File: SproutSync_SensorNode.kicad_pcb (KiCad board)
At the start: 4 copper layers, 41 x 82.3 mm, 53 parts, among them J1 10132798-031100LF, J2 10132798-031100LF, J3 OSTVN04A150, J4 3-2199250-4, J5 3-2199250-4, J6 OSTVN02A150, J7 Conn_01x03, Q1 PMH950UPEH, Q2 AS2302, Q3 PMH950UPEH, Q5 PMH950UPEH, U1 LTR-329ALS-01, U2 SHT40-AD1F-R2, U3 ZMOD4410AI1R, U4 SN75176BDR, U5 AP63205WU-7, U7 MCP1700T-3302E/TT, U8 74HC04D

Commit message: 2nd rev schematic done
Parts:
- moved C9 36.1 mm to (101.9, 114.7)
- moved U7 35.2 mm to (101.8, 112.3)
- moved C10 35.2 mm to (99.2, 112.2)
- moved D4 31.4 mm to (83.3, 105.2)
- moved D5 31.4 mm to (83.3, 104.0)
- moved R2 31.4 mm to (81.2, 105.2)
- moved R6 31.4 mm to (81.2, 104.0)
- moved U3 10.6 mm to (106.6, 109.7)
- moved Q3 9.95 mm to (103.8, 110.6), turned to 0 degrees
- moved C2 7.49 mm to (107.5, 112.0), turned to 180 degrees
- moved U1 5.01 mm to (112.2, 109.4), turned to 90 degrees
- moved C8 4.63 mm to (119.1, 93.2)
- moved U2 4.39 mm to (109.6, 109.6), turned to -90 degrees
- moved C1 4.09 mm to (112.7, 111.5), turned to 0 degrees
- moved R3 1.61 mm to (111.3, 104.1)
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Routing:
- net /PetalStackingConectors/PAD32: track 1.15 -> 35.8 mm
- net /PetalStackingConectors/PAD33: track 1.64 -> 31.0 mm
- net +5V: track 15.2 -> 36.9 mm
- net Sns_3p3: track 0.00 -> 18.7 mm
- net /PetalStackingConectors/PAD30: track 0.00 -> 18.4 mm
- net WRT_ENA: track 0.00 -> 14.6 mm
- net /PetalStackingConectors/PAD31: track 0.00 -> 13.6 mm
- net D: track 0.00 -> 11.6 mm
- net RS485_B-: track 0.00 -> 10.6 mm
- net R: track 0.00 -> 10.2 mm
- net RS485_A+: track 0.00 -> 9.54 mm
- net RX: track 0.00 -> 8.55 mm
- net TX: track 0.00 -> 6.00 mm
- net +3V3: track 0.00 -> 5.85 mm
- net RE/DE: track 0.00 -> 5.17 mm
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
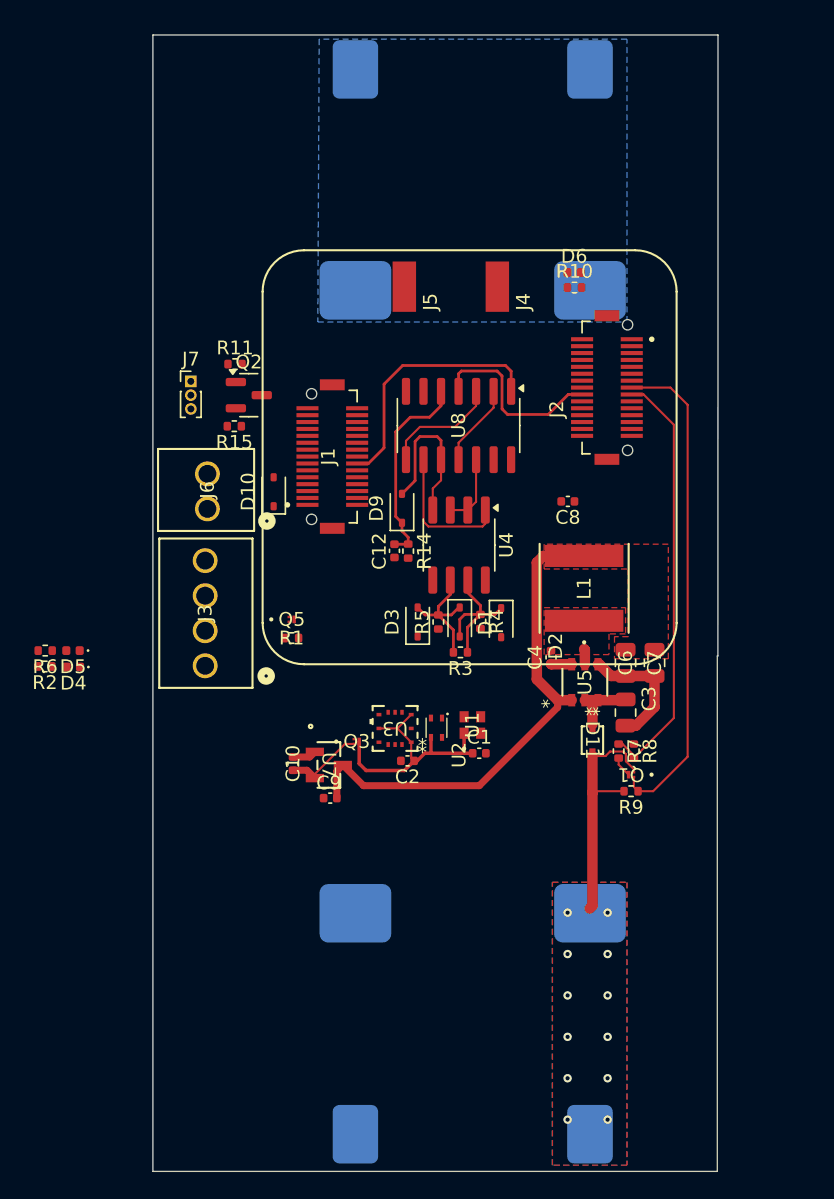
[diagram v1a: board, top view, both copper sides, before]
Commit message: mostly routed
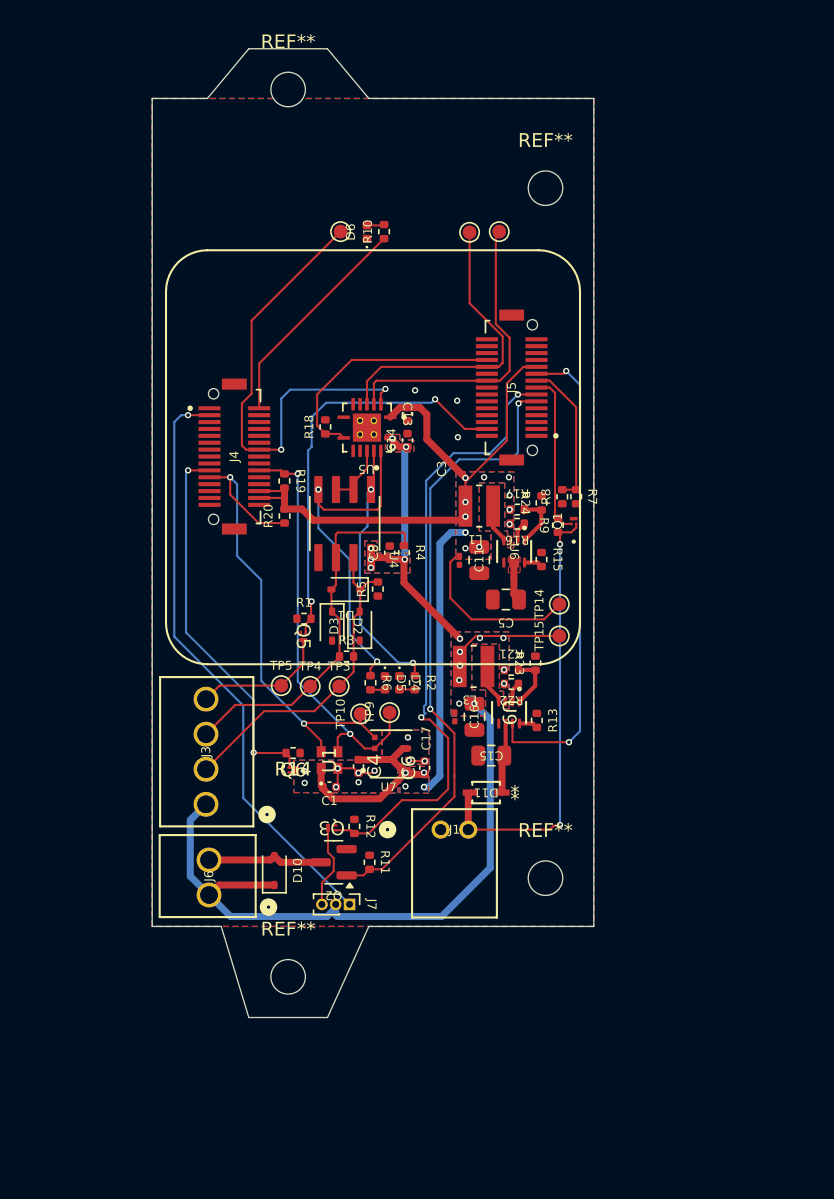
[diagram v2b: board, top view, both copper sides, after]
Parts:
- removed BT2, BT3: Battery_Cell, SproutSenseFootprints:Keystone_18650_Holder
- removed C10, C2, C9: 1uF, Capacitor_SMD:C_0402_1005Metric
- removed C12: 100nF, Capacitor_SMD:C_0402_1005Metric
- removed C7: 22uF, Capacitor_SMD:C_0805_2012Metric
- removed D9: 1N4148WS, Diode_SMD:D_SOD-323
- removed J2: 10132798-031100LF, SproutSenseFootprints:AMPHENOL_10132798-031100LF
- removed U2: SHT40-AD1F-R2, SproutSenseFootprints:SHT4X
- removed U3: ZMOD4410AI1R, SproutSenseFootprints:QFN_410AI1R_REN
- removed U8: 74HC04D, Package_SO:SOIC-14_3.9x8.7mm_P1.27mm
- added C11: 22uF, Capacitor_SMD:C_0805_2012Metric, F.Cu at (112.7, 97.5)
- added C13: 1uF, Capacitor_SMD:C_0402_1005Metric, F.Cu at (107.5, 86.9)
- added C14: 1uF, Capacitor_SMD:C_0402_1005Metric, F.Cu at (107.5, 88.8)
- added C15: 22uF, Capacitor_SMD:C_0805_2012Metric, F.Cu at (113.6, 111.6)
- added C16: 22uF, Capacitor_SMD:C_0805_2012Metric, F.Cu at (112.4, 108.8)
- added C17: 10n, Capacitor_SMD:C_0201_0603Metric, F.Cu at (110.9, 108.8)
- added C5: 22uF, Capacitor_SMD:C_0805_2012Metric, F.Cu at (114.6, 100.3)
- added L3: 2.2u, SproutSenseFootprints:IND_VLS3012CX-2R2M-1, F.Cu at (112.3, 105.2)
- added Q6: SIUD412ED-T1-GE3, SproutSenseFootprints:SMT_412ED-T1-GE3_VIS, F.Cu at (99.2, 112.7)
- added R12: 4.7k, Resistor_SMD:R_0402_1005Metric, F.Cu at (103.7, 116.8)
- added R13: 9.31k, Resistor_SMD:R_0402_1005Metric, F.Cu at (116.9, 109.1)
- added R16: 100k, Resistor_SMD:R_0402_1005Metric, F.Cu at (115.5, 94.8)
- added R17: 154k, Resistor_SMD:R_0402_1005Metric, F.Cu at (115.5, 93.8)
- added R18: 4.7k, Resistor_SMD:R_0402_1005Metric, F.Cu at (101.5, 87.8)
- added R19: 4.7k, Resistor_SMD:R_0402_1005Metric, F.Cu at (98.6, 91.7)
- added R20: 4.7k, Resistor_SMD:R_0402_1005Metric, F.Cu at (98.6, 94.3)
- added R21: 249k, Resistor_SMD:R_0402_1005Metric, F.Cu at (115.0, 105.4)
- added R22: 100k, Resistor_SMD:R_0402_1005Metric, F.Cu at (115.0, 106.4)
- added R23: 34k, Resistor_SMD:R_0402_1005Metric, F.Cu at (116.8, 104.9)
- added R24: 34k, Resistor_SMD:R_0402_1005Metric, F.Cu at (117.2, 93.3)
- added REF**: MountingHole_2.5mm, MountingHole:MountingHole_2.5mm, F.Cu at (98.8, 127.7)
- added REF**: MountingHole_2.5mm, MountingHole:MountingHole_2.5mm, F.Cu at (98.8, 63.4)
- added REF**: MountingHole_2.5mm, MountingHole:MountingHole_2.5mm, F.Cu at (117.5, 120.5)
- added REF**: MountingHole_2.5mm, MountingHole:MountingHole_2.5mm, F.Cu at (117.5, 70.5)
- added TP1: TestPoint, TestPoint:TestPoint_Pad_D1.0mm, F.Cu at (114.2, 73.7)
- added TP10: TestPoint, TestPoint:TestPoint_Pad_D1.0mm, F.Cu at (104.1, 108.6)
- added TP14: TestPoint, TestPoint:TestPoint_Pad_D1.0mm, F.Cu at (118.5, 100.7)
- added TP15: TestPoint, TestPoint:TestPoint_Pad_D1.0mm, F.Cu at (118.5, 103.0)
- added TP2: TestPoint, TestPoint:TestPoint_Pad_D1.0mm, F.Cu at (102.7, 73.7)
- added TP3: TestPoint, TestPoint:TestPoint_Pad_D1.0mm, F.Cu at (102.5, 106.6)
- added TP4: TestPoint, TestPoint:TestPoint_Pad_D1.0mm, F.Cu at (100.5, 106.6)
- added TP5: TestPoint, TestPoint:TestPoint_Pad_D1.0mm, F.Cu at (98.3, 106.5)
- added TP6: TestPoint, TestPoint:TestPoint_Pad_D1.0mm, F.Cu at (112.0, 73.7)
- added TP9: TestPoint, TestPoint:TestPoint_Pad_D1.0mm, F.Cu at (106.2, 108.5)
- added U6: TPS629203DRL, SproutSenseFootprints:SOT5X3-8_DRL_TEX, F.Cu at (115.2, 96.8)
- added U9: TPS629206DRLR, SproutSenseFootprints:SOT5X3-8_DRL_TEX, F.Cu at (114.9, 108.5)
- C3: value 22uF -> 10n; footprint Capacitor_SMD:C_0805_2012Metric -> Capacitor_SMD:C_0201_0603Metric
- C6: value 22uF -> 100nF; footprint Capacitor_SMD:C_0805_2012Metric -> Capacitor_SMD:C_0402_1005Metric
- C8: value 100nF -> 1uF
- J1: value 10132798-031100LF -> S2B-PH-K-S; footprint SproutSenseFootprints:AMPHENOL_10132798-031100LF -> SproutSenseFootprints:CONN_S2B-PH-K-S_JST
- J4, J5: value 3-2199250-4 -> 10132797-031100LF; footprint SproutSenseFootprints:TE_3-2199250-4 -> SproutSenseFootprints:AMPHENOL_10132797-031100LF
- L1: value 4.7uH -> 2.2u; footprint SproutSenseFootprints:IND_TAIYO_NRS6028_TAY -> SproutSenseFootprints:IND_VLS3012CX-2R2M-1
- Q3, Q5: value PMH950UPEH -> SIUD412ED-T1-GE3; footprint SproutSenseFootprints:QPMOS1G2S3d_SOT8001_NEX -> SproutSenseFootprints:SMT_412ED-T1-GE3_VIS
- R10, R2, R6: value 4.7k -> 1k
- R14: value 22k -> 4.7k
- R15, R7: value 4.7k -> 7.5k
- U4: value SN75176BDR -> SN65HVD3082EDR; footprint Package_SO:SOP-8_3.76x4.96mm_P1.27mm -> SproutSenseFootprints:SOIC127P599X175-8N
- U5: value AP63205WU-7 -> TXB0104RGYR; footprint SproutSenseFootprints:SOIC_05WU-7_DIO -> SproutSenseFootprints:QFN50P350X350X100-15N
- U7: value MCP1700T-3302E/TT -> BME688; footprint SproutSenseFootprints:SOT-23_MC_MCH -> SproutSenseFootprints:IC_BME688
- moved J7 39.6 mm to (103.3, 122.4), turned to -90 degrees
- moved R11 37.4 mm to (104.8, 119.3), turned to 90 degrees
- moved Q2 34.4 mm to (102.2, 119.3), turned to 180 degrees
- moved J1 28.2 mm to (109.9, 117.0), turned to 0 degrees
- moved J6 28.0 mm to (93.1, 121.7)
- moved D10 27.5 mm to (97.8, 120.0)
- moved R2 26.8 mm to (108.0, 106.3), turned to -90 degrees
- moved U5 24.3 mm to (104.6, 87.8), turned to 180 degrees
- moved R15 24.3 mm to (117.2, 97.4), turned to -90 degrees
- moved R6 23.7 mm to (104.8, 106.3), turned to -90 degrees
- moved D4 23.7 mm to (106.9, 106.3), turned to -90 degrees
- moved D5 22.7 mm to (105.9, 106.3), turned to -90 degrees
- moved J4 22.7 mm to (95.0, 90.0), turned to 90 degrees
- moved R9 20.0 mm to (118.4, 94.9), turned to -90 degrees
- moved R8 19.1 mm to (118.7, 92.9), turned to 90 degrees
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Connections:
- C1 pad 1: Sns_3p3 -> +3V3
- C1 pad 2: GND -> AMB_LOW_SW
- C3 pad 1: +BATT -> +3V3
- C4 pad 1: Net-(U5-BST) -> +3V3
- C4 pad 2: Net-(U5-SW) -> AMB_LOW_SW
- C6 pad 1: +5V -> +3V3
- C6 pad 2: GND -> AMB_LOW_SW
- D1 pad 1: RS485_A+ -> RS485_B-
- D1 pad 2: RS485_B- -> RS485_A+
- D2 pad 1: RS485_B- -> RS485_A+
- D3 pad 2: RS485_A+ -> RS485_B-
- J1 pad 1: unconnected-(J1-Pad1) -> GND
- J1 pad 2: /PetalStackingConectors/PAD14 -> /Power/BAT_POS
- J3 pad 1: Net-(J3-Pin_1) -> +5V
- J3 pad 4: GND -> Net-(J3-Pin_4)
- J4 pad 1: Net-(AE2-Pad1) -> unconnected-(J4-Pad1)
- J5 pad 1: GND -> /PetalStackingConectors/PAD4
- J7 pad 3: GND -> Net-(J7-Pin_3)
- L1 pad 1: Net-(U5-SW) -> Net-(U6-SW)
- L1 pad 2: +5V -> +3V3
- Q2 pad 2: Net-(Q2-S) -> GND
- Q3 pad 1: /AmbientSensors/~{nAMBSNS_ENA} -> /PetalStackingConectors/PAD15
- Q3 pad 2: +3V3 -> GND
- Q3 pad 3: Sns_3p3 -> Net-(J7-Pin_3)
- Q5 pad 2: +5V -> GND
- Q5 pad 3: Net-(J3-Pin_1) -> Net-(J3-Pin_4)
- R1 pad 1: /PetalStackingConectors/PAD29 -> GND
- R1 pad 2: +5V -> /PetalStackingConectors/PAD29
- R14 pad 1: WRT_ENA -> GND
- R14 pad 2: GND -> /PetalStackingConectors/PAD7
- R15 pad 2: Net-(Q2-S) -> Net-(U6-MODE/S-CONF)
- R3 pad 1: RS485_B- -> RS485_A+
- R3 pad 2: RS485_A+ -> RS485_B-
- R4 pad 1: RS485_B- -> RS485_A+
- R5 pad 2: RS485_A+ -> RS485_B-
- U1 pad 1: Sns_3p3 -> +3V3
- U1 pad 2: GND -> AMB_LOW_SW
- U4 pad 1: R -> RX
- U4 pad 4: D -> TX
- U5 pad 1: +5V -> +3V3
- U5 pad 2: +BATT -> /PetalStackingConectors/PAD30
- U5 pad 3: +BATT -> /PetalStackingConectors/PAD31
- U5 pad 4: GND -> /PetalStackingConectors/PAD1
- U5 pad 5: Net-(U5-SW) -> unconnected-(U5-A4-Pad5)
- U5 pad 6: Net-(U5-BST) -> unconnected-(U5-NC_6-Pad6)
- U7 pad 1: GND -> AMB_LOW_SW
- U7 pad 3: +5V -> /PetalStackingConectors/PAD49
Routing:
- net +3V3: track 5.85 -> 89.1 mm, vias 0 -> 15
- net /PetalStackingConectors/PAD13: track 0.00 -> 45.6 mm, vias 0 -> 2
- net /PetalStackingConectors/PAD15: track 0.00 -> 45.2 mm, vias 0 -> 2
- net /PetalStackingConectors/PAD14: track 0.00 -> 43.0 mm, vias 0 -> 1
- net +5V: track 36.9 -> 76.0 mm, vias 0 -> 17
- net /PetalStackingConectors/PAD48: track 0.00 -> 36.5 mm, vias 0 -> 2
- net /PetalStackingConectors/PAD35: track 0.00 -> 35.3 mm, vias 0 -> 2
- net /PetalStackingConectors/PAD49: track 0.00 -> 30.6 mm, vias 0 -> 2
- net /PetalStackingConectors/PAD29: track 0.00 -> 30.2 mm, vias 0 -> 2
- net /PetalStackingConectors/PAD7: track 0.00 -> 27.6 mm, vias 0 -> 2
- net /PetalStackingConectors/PAD32: track 35.8 -> 11.8 mm
- net /PetalStackingConectors/PAD1: track 0.00 -> 22.5 mm
- net /PetalStackingConectors/PAD33: track 31.0 -> 10.7 mm
- net TX: track 6.00 -> 25.3 mm, vias 0 -> 2
- net Sns_3p3: track 18.7 -> 0.00 mm
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- added copper zone on B.Cu, net +3V3
- added copper zone on F.Cu, net +3V3
- added copper zone on B.Cu, net +5V
- added copper zone on F.Cu, net +BATT
- added copper zone on B.Cu, net AMB_LOW_SW
- added copper zone on F.Cu, net AMB_LOW_SW
- added copper zone on B.Cu, net GND
- added copper zone on F.Cu, net GND
- removed copper zone on B.Cu, net /Power/BAT_MID
- removed copper zone on B.Cu, net /Power/BAT_POS
- removed copper zone on F.Cu, net /Power/BAT_POS
- removed copper zone on F.Cu, net Net-(U5-SW)
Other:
- board size 41 x 82.3 mm -> 32 x 70.2 mm
- copper layers 4 -> 2

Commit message: edited silksceen
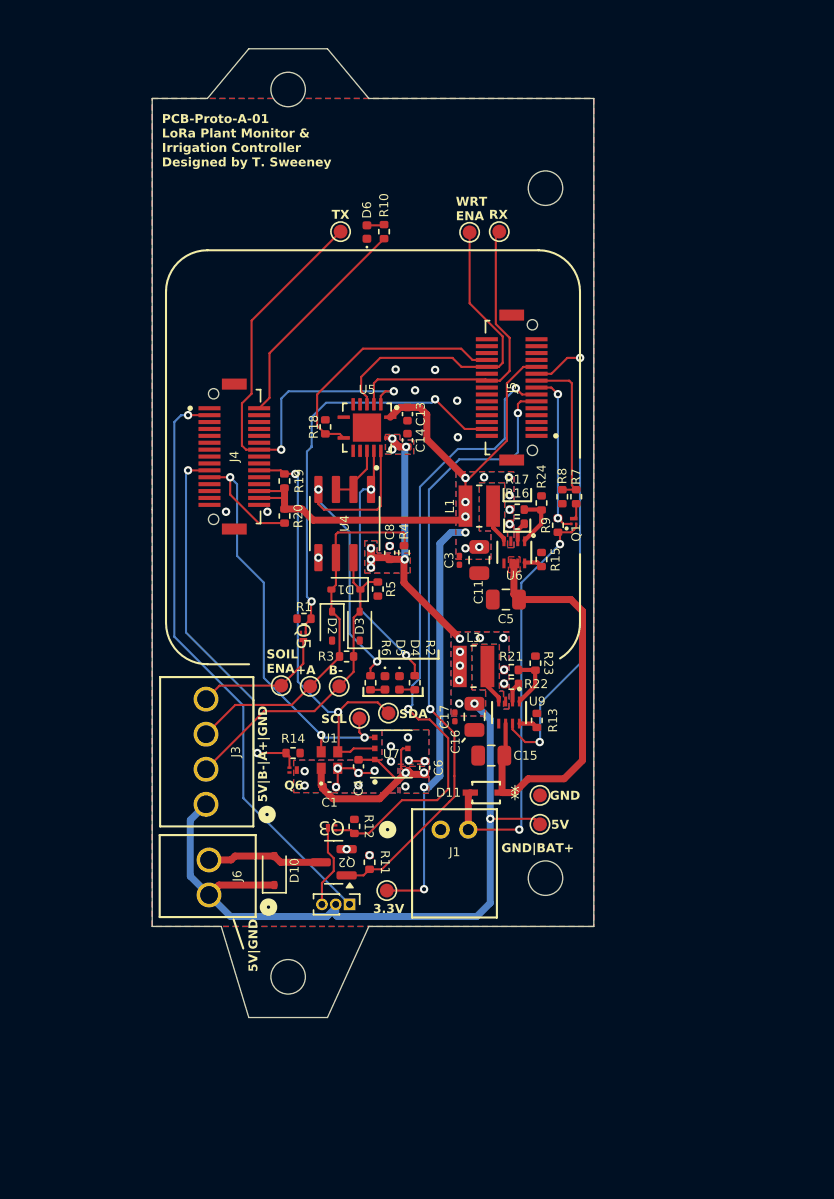
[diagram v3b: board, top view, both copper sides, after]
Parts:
- added TP7: TestPoint, TestPoint:TestPoint_Pad_D1.0mm, F.Cu at (117.1, 114.5)
- moved TP14 24.2 mm to (106.0, 121.4)
- moved TP15 13.7 mm to (117.1, 116.6)
- moved TP10 0.33 mm to (104.0, 108.9)
- moved TP9 0.09 mm to (106.1, 108.5)
- moved U6 0.06 mm to (115.2, 96.9)
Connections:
- J4 pad 13: +5V -> unconnected-(J4-Pad13)
- J4 pad 14: +5V -> unconnected-(J4-Pad14)
- J5 pad 13: /PetalStackingConectors/V_BAT -> unconnected-(J5-Pad13)
- J5 pad 14: /PetalStackingConectors/V_BAT -> unconnected-(J5-Pad14)
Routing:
- net +BATT: track 7.96 -> 30.5 mm
- net +5V: track 76.0 -> 73.6 mm, vias 17 -> 18
- net +3V3: track 89.1 -> 87.2 mm, vias 15 -> 16
- net /PetalStackingConectors/PAD15: track 45.2 -> 46.8 mm
- net /Power/BAT_POS: track 32.5 -> 31.0 mm
- net /PetalStackingConectors/PAD1: track 22.5 -> 23.8 mm
- net /PetalStackingConectors/PAD49: track 30.6 -> 32.0 mm
- net Net-(Q1-D): track 0.00 -> 1.15 mm
- net /PetalStackingConectors/PAD30: track 34.2 -> 35.2 mm
- net /PetalStackingConectors/PAD33: track 10.7 -> 11.5 mm
- net /PetalStackingConectors/PAD2: track 17.9 -> 18.6 mm
- net /PetalStackingConectors/PAD48: track 36.5 -> 36.0 mm, vias 2 -> 3
- net /PetalStackingConectors/PAD32: track 11.8 -> 11.9 mm, vias 0 -> 2
- net GND: vias 3 -> 11
- net AMB_LOW_SW: vias 10 -> 12
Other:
- board text added: "3.3V"
- board text added: "5V"
- board text added: "5V|B-|A+|GND"
- board text added: "5V|GND"
- board text added: "A+"
- board text added: "B-"
- board text added: "GND"
- board text added: "GND|BAT+"
- board text added: "PCB-Proto-A-01 LoRa Plant Monitor & Irrigation Controller Designed by T. Sweeney"
- board text added: "RX"
- board text added: "SCL"
- board text added: "SDA"
- board text added: "SOIL ENA"
- board text added: "TX"
- board text added: "WRT ENA"

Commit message: finished rev1
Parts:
- added R25: 100m, Resistor_SMD:R_0603_1608Metric, F.Cu at (117.1, 112.7)
- added TP11: TestPoint, TestPoint:TestPoint_Pad_D1.0mm, F.Cu at (119.8, 110.8)
- added TP8: TestPoint, TestPoint:TestPoint_Pad_D1.0mm, F.Cu at (119.7, 113.6)
- moved TP1 4.60 mm to (109.5, 73.7)
- moved R13 0.57 mm to (116.8, 108.5)
- moved C15 0.39 mm to (113.2, 111.5)
- moved TP7 0.10 mm to (117.1, 114.6)
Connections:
- D11 pad 1: +BATT -> Net-(D11-Pad1)
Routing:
- net Net-(D11-Pad1): track 0.00 -> 7.05 mm
- net +BATT: track 30.5 -> 25.3 mm
- net /PetalStackingConectors/PAD13: track 45.7 -> 48.7 mm
- net /PetalStackingConectors/PAD1: track 23.8 -> 21.9 mm, vias 0 -> 2
- net /PetalStackingConectors/PAD31: track 22.4 -> 20.8 mm, vias 0 -> 2
- net Net-(U9-FB/VSET): track 3.95 -> 5.29 mm
- net /PetalStackingConectors/PAD32: track 11.9 -> 12.8 mm
- net Net-(U6-FB/VSET): track 3.95 -> 4.59 mm
- net +3V3: track 87.2 -> 87.8 mm
- net GND: vias 11 -> 54
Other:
- outline, holes or cut-outs redrawn
- board text added: "0"
- board text added: "0 mm"
- board text added: "0.01 mm"
- board text added: "0.02"
- board text added: "0.035 mm"
- board text added: "1"
- board text added: "1.51 mm"
- board text added: "3.3"
- board text added: "4.5"
- board text added: "B.Cu"
- board text added: "B.Mask"
- board text added: "B.Paste"
- board text added: "B.Silkscreen"
- board text added: "Bottom Silk Screen"
- board text added: "Bottom Solder Mask"
- board text added: "Bottom Solder Paste"
- board text added: "Color"
- board text added: "Dielectric"
- board text added: "Epsilon R"
- board text added: "F.Cu"
- board text added: "F.Mask"
- board text added: "F.Paste"
- board text added: "F.Silkscreen"
- board text added: "FR4"
- board text added: "Layer Name"
- board text added: "Loss Tangent"
- board text added: "Material"
- board text added: "Not specified"
- board text added: "PCB-Proto-A-01 LoRa Plant Monitor & Irrigation Controller"
- board text added: "SNS+"
- board text added: "SNS-"
- board text added: "Thickness (mm)"
- board text added: "Top Silk Screen"
- board text added: "Top Solder Mask"
- board text added: "Top Solder Paste"
- board text added: "Type"
- board text added: "copper"
- board text added: "core"
- board text removed: "PCB-Proto-A-01 LoRa Plant Monitor & Irrigation Controller Designed by T. Sweeney"
